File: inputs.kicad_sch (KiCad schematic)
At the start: 0 parts

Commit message: big commit with power and inputs
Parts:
- added C10, C11, C12, C13, C14, C15, C16, C5, C6, C7, C8, C9: 0.1uF, Capacitor_SMD:C_0603_1608Metric, symbol Device:C
- added C17: 1uF, Capacitor_SMD:C_0603_1608Metric, symbol Device:C
- added J1: TPS43, footprints:TPS43_wires, symbol Connector_Generic:Conn_01x06
- added R10, R12, R14, R16, R18, R20, R22, R23, R26, R27, R30, R6, R8: 100k, Resistor_SMD:R_0603_1608Metric, symbol Device:R
- added R11, R13, R15, R17, R19, R21, R24, R25, R28, R29, R31, R7, R9: 10k, Resistor_SMD:R_0603_1608Metric, symbol Device:R
- added SW1: KEY_A, footprints:CPG135001D02, symbol user:Kailh_Choc
- added SW10, SW11, SW12, SW7, SW8, SW9: D2F-01F, footprints:D2F01F, symbol user:D2F-01F
- added SW13: RKB2SJM250SMTR LFS, footprints:RKB2SJM250SMTRLFS, symbol Switch:SW_Push
- added SW2: KEY_B, footprints:CPG135001D02, symbol user:Kailh_Choc
- added SW3: KEY_C, footprints:CPG135001D02, symbol user:Kailh_Choc
- added SW4: KEY_D, footprints:CPG135001D02, symbol user:Kailh_Choc
- added SW5: KEY_E, footprints:CPG135001D02, symbol user:Kailh_Choc
- added SW6: KEY_F, footprints:CPG135001D02, symbol user:Kailh_Choc
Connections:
- new net: R22.2, R24.1, SW9.1 (COM)
- new net: R8.2, R9.1, SW2.2
- new net: R16.2, R17.1, SW6.2
- new net: R23.2, R25.1, SW10.1 (COM)
- new net: R10.2, R11.1, SW3.2
- new net: R12.2, R13.1, SW4.2
- new net: R6.2, R7.1, SW1.2
- new net: R18.2, R19.1, SW7.1 (COM)
- new net: R20.2, R21.1, SW8.1 (COM)
- new net: R27.2, R29.1, SW12.1 (COM)
- new net: R14.2, R15.1, SW5.2
- new net: R26.2, R28.1, SW11.1 (COM)
- new net: R30.2, R31.1, SW13.2
- new net +3V0: J1.4 (Pin_4), R10.1, R12.1, R14.1, R16.1, R18.1, R20.1, R22.1, R23.1, R26.1, R27.1, R30.1, R6.1, R8.1
- new net EXT_~{RST}: C17.1, R31.2
- new net GND: C10.2, C11.2, C12.2, C13.2, C14.2, C15.2, C16.2, C17.2, C5.2, C6.2, C7.2, C8.2, C9.2, J1.3 (Pin_3), SW1.1, SW1.MH2, SW1.MH3, SW10.2 (NO), SW11.2 (NO), SW12.2 (NO), SW13.1, SW2.1, SW2.MH2, SW2.MH3, SW3.1, SW3.MH2, SW3.MH3, SW4.1, SW4.MH2, SW4.MH3, SW5.1, SW5.MH2, SW5.MH3, SW6.1, SW6.MH2, SW6.MH3, SW7.2 (NO), SW8.2 (NO), SW9.2 (NO)
- new net KEY_A: C5.1, R7.2
- new net KEY_B: C6.1, R9.2
- new net KEY_C: C7.1, R11.2
- new net KEY_D: C8.1, R13.2
- new net KEY_E: C9.1, R15.2
- new net KEY_F: C10.1, R17.2
- new net MOUSE_1A: C11.1, R19.2
- new net MOUSE_1B: C12.1, R21.2
- new net MOUSE_2A: C13.1, R24.2
- new net MOUSE_2B: C14.1, R25.2
- new net MOUSE_3A: C15.1, R28.2
- new net MOUSE_3B: C16.1, R29.2
- new net TP_RDY: J1.1 (Pin_1)
- new net TP_SCL: J1.5 (Pin_5)
- new net TP_SDA: J1.2 (Pin_2)
- new net TP_~{RST}: J1.6 (Pin_6)
- no-connect marks 0 -> 6

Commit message: schema functionally done
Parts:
- added C36, C37: 1uF, Capacitor_SMD:C_0603_1608Metric, symbol Device:C
- added R32, R37: 100k, Resistor_SMD:R_0603_1608Metric, symbol Device:R
- added R35, R38: 10k, Resistor_SMD:R_0603_1608Metric, symbol Device:R
- added SW14, SW15: RKB2SJM250SMTR LFS, footprints:RKB2SJM250SMTRLFS, symbol Switch:SW_Push
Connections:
- net +3V0: now also R32.1, R37.1
- net GND: now also C36.2, C37.2, SW14.1, SW15.1
- net EXT_~{RST} renamed ~{EXT_RST}
- new net: R32.2, R35.1, SW14.2
- new net: R37.2, R38.1, SW15.2
- new net MENU: C37.1, R38.2
- new net ~{USB_BOOT}: C36.1, R35.2
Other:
- moved on the sheet: C10, C11, C12, C13, C14, C15, C16, C17, C5, C6, C7, C8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

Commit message: reannotation
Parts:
- renumbered C5 to C25, C6 to C26, C7 to C27, C8 to C28, C9 to C29, C10 to C30, C11 to C31, C12 to C32, C13 to C33, C14 to C34, C15 to C35, C16 to C36, C17 to C38, C36 to C39, J1 to J4, R6 to R17, R8 to R18, R10 to R19, R12 to R20, R14 to R21, R16 to R22, R7 to R23, R9 to R24, R11 to R25, R13 to R26, R15 to R27, R17 to R28, R18 to R29, R20 to R30, R22 to R31, R23 to R32, R26 to R33, R27 to R34, R19 to R35, R21 to R36, R24 to R37, R25 to R38, R28 to R39, R29 to R40, R37 to R41, R30 to R42, R32 to R43, R38 to R44, R31 to R45, R35 to R46, SW15 to SW13, SW13 to SW14, SW14 to SW15

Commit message: change 0603 to 0805
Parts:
- C25, C26, C27, C28, C29, C30, C31, C32, C33, C34, C35, C36, C37, C38, C39: footprint Capacitor_SMD:C_0603_1608Metric -> Capacitor_SMD:C_0805_2012Metric
- R17, R18, R19, R20, R21, R22, R23, R24, R25, R26, R27, R28, R29, R30, R31, R32, R33, R34, R35, R36, R37, R38, R39, R40, R41, R42, R43, R44, R45, R46: footprint Resistor_SMD:R_0603_1608Metric -> Resistor_SMD:R_0805_2012Metric

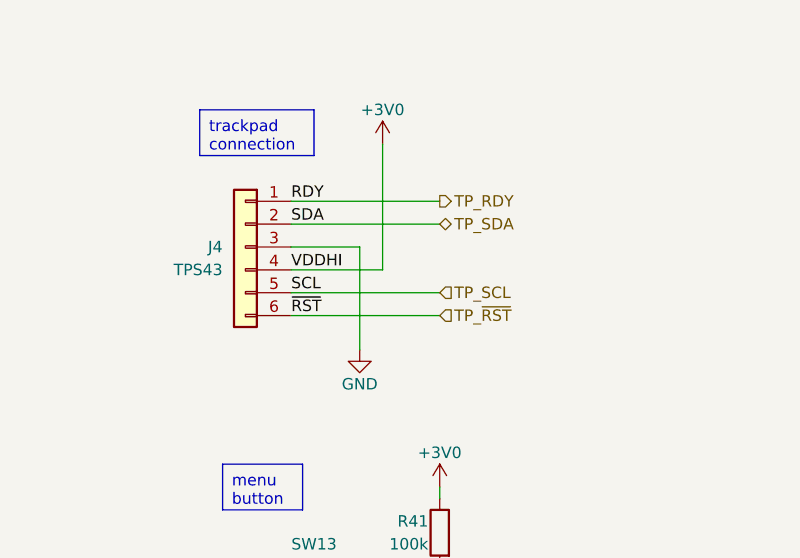
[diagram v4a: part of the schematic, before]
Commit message: add external modules
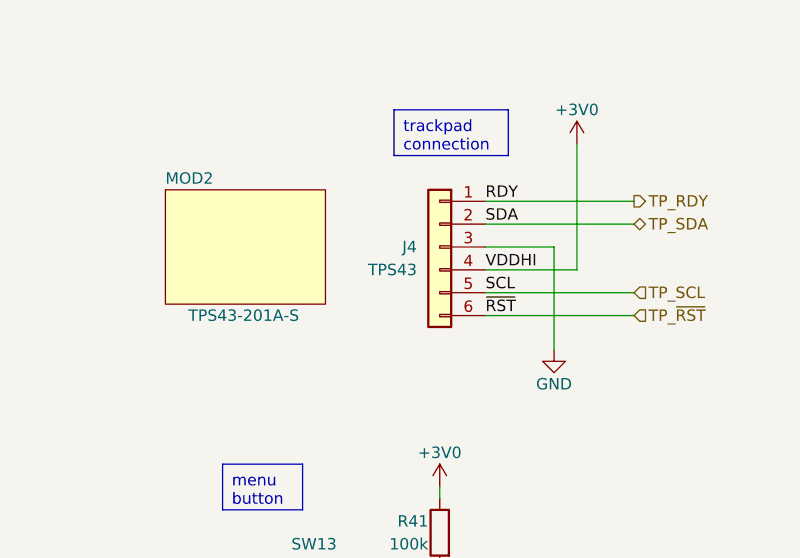
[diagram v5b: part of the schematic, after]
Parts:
- added MOD2: TPS43-201A-S, footprints:TPS43, symbol user:TPS43-201A-S
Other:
- moved on the sheet: J4

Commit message: schematic cleanup
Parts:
- removed C38, C39: 1uF, Capacitor_SMD:C_0805_2012Metric, symbol Device:C
- removed R42, R43: 100k, Resistor_SMD:R_0805_2012Metric, symbol Device:R
- removed R45, R46: 10k, Resistor_SMD:R_0805_2012Metric, symbol Device:R
- removed SW11, SW12: D2F-01F, footprints:D2F01F, symbol user:D2F-01F
- removed SW14, SW15: RKB2SJM250SMTR LFS, footprints:RKB2SJM250SMTRLFS, symbol Switch:SW_Push
- added C42, C43: 0.1uF, Capacitor_SMD:C_0805_2012Metric, symbol Device:C
- added R47, R48: 100k, Resistor_SMD:R_0805_2012Metric, symbol Device:R
- added R49, R50: 10k, Resistor_SMD:R_0805_2012Metric, symbol Device:R
- added SW11, SW12: RKB2SJM250SMTR, footprints:RKB2SJM250SMTRLFS, symbol Switch:SW_Push
- added SW16, SW17: D2F-01F, footprints:D2F01F, symbol user:D2F-01F
- C35, C36: value 0.1uF -> 1uF
- R19, R22, R31, R32: value 100k -> 10k
- R25, R26, R37, R39: value 10k -> 100k
- SW13: value RKB2SJM250SMTR LFS -> RKB2SJM250SMTR; Input (none) -> MENU
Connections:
- net +3V0: now also R25.1, R26.1, R37.1, R39.1, R47.1, R48.1; no longer R19.1, R22.1, R31.1, R32.1
- net GND: now also C42.2, C43.2, SW11.1, SW12.1, SW16.2 (NO), SW17.2 (NO)
- net KEY_B: now also R19.2; no longer R24.2
- net KEY_C: now also R22.2; no longer R25.2
- net KEY_D: now also R24.2; no longer R26.2
- net MENU: now also C35.1, R38.2; no longer C37.1, R44.2
- net MOUSE_1A: now also C32.1, R31.2; no longer C31.1, R35.2
- net MOUSE_1B: now also C31.1, R32.2; no longer C32.1, R36.2
- net MOUSE_2A: now also R35.2; no longer R37.2
- net MOUSE_2B: now also R36.2; no longer R38.2
- net MOUSE_3A: now also C42.1, R49.2; no longer C35.1, R39.2
- net MOUSE_3B: now also C43.1, R50.2; no longer C36.1, R40.2
- net ~{EXT_RST}: now also C36.1, R40.2
- net ~{USB_BOOT}: now also C37.1, R44.2
- net at R18.2, SW2.2: now also R19.1; no longer R24.1
- net at R28.1, SW6.2: now also R26.2; no longer R22.2
- net at R34.2: now also R36.1, SW10.1 (COM); no longer R40.1
- net at R27.1, SW5.2: now also R25.2; no longer R21.2
- net at R33.2: now also R35.1, SW9.1 (COM); no longer R39.1
- net at R41.2, R44.1: now also SW12.2; no longer SW13.2
- new net: R48.2, R50.1, SW17.1 (COM)
- new net: R30.2, R31.1, SW7.1 (COM)
- new net: R37.2, R38.1, SW13.2
- new net: R20.2, R22.1, SW3.2
- new net: R47.2, R49.1, SW16.1 (COM)
- new net: R21.2, R24.1, SW4.2
- new net: R39.2, R40.1, SW11.2
- new net: R29.2, R32.1, SW8.1 (COM)
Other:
- note added: "extra buttons"
- note added: "keyboard switches"
- note added: "mouse buttons"
- note added: "trackpad"
- moved on the sheet: C25, J4, MOD2, R17, R23, SW1, SW13, SW7
